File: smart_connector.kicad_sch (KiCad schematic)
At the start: 0 parts

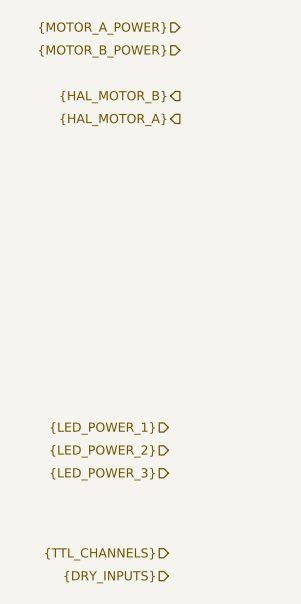
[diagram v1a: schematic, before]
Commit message: Add power stages
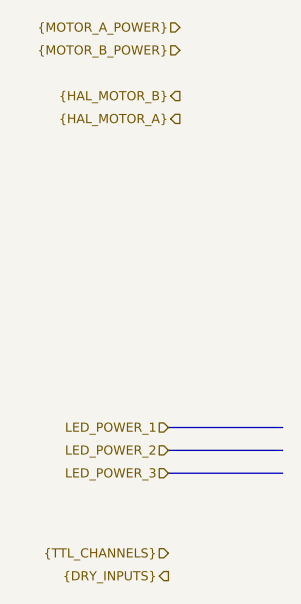
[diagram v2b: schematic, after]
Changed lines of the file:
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@@
 	(generator_version "9.0")
 	(paper "A4")
+	(bus
+		(pts
+			(xy 72.39 100.33) (xy 85.09 100.33)
+		)
+		(stroke
+			(width 0)
+			(type default)
+		)
+	)
+	(bus
+		(pts
+			(xy 72.39 95.25) (xy 85.09 95.25)
+		)
+		(stroke
+			(width 0)
+			(type default)
+		)
+	)
+	(bus
+		(pts
+			(xy 72.39 97.79) (xy 85.09 97.79)
+		)
+		(stroke
+			(width 0)
+			(type default)
+		)
+	)
 	(hierarchical_label "{MOTOR_B_POWER}"
 		(shape input)
@@
 		)
 	)
-	(hierarchical_label "{LED_POWER_1}"
+	(hierarchical_label "LED_POWER_1"
 		(shape input)
 		(at 72.39 95.25 180)
@@
 		)
 	)
-	(hierarchical_label "{LED_POWER_2}"
+	(hierarchical_label "LED_POWER_2"
 		(shape input)
 		(at 72.39 97.79 180)
@@
 		)
 	)
-	(hierarchical_label "{LED_POWER_3}"
+	(hierarchical_label "LED_POWER_3"
 		(shape input)
 		(at 72.39 100.33 180)
@@
 	)
 	(hierarchical_label "{DRY_INPUTS}"
-		(shape input)
+		(shape output)
 		(at 72.39 111.76 180)
 		(effects
